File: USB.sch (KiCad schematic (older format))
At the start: 74 parts, among them J10 10103594-0001LF, Q14 BSS138LT1G, Q18 BSS138LT1G, Q24 BSS138LT1G, Q6 BSS138LT1G, U15 SN74AVC2T245RSWR, U21 M93C46-WMN6TP, U22 TLV62565DBVT, U23 FT4232H-56Q, U24 SN74AVC2T245RSWR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

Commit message: fixed bugs
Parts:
- D13: symbol AMC_FMC_Carrier-PcbDoc-rescue:PRTR5V0U2X-Diodes-AMC_FMC_Carrier-PcbDoc-rescue-AMC_FMC_Carrier-PcbDoc-rescue -> AMC_FMC_Carrier-PcbDoc-rescue:PRTR5V0U2X-Diodes-AMC_FMC_Carrier-PcbDoc-rescue-AMC_FMC_Carrier-PcbDoc-rescue-AMC_FMC_Car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
- J10: symbol AMC_FMC_Carrier-PcbDoc-rescue:HIROSE_ZX62RD-AB-5P8-Miscellaneous-AMC_FMC_Carrier-PcbDoc-rescue-AMC_FMC_Carrier-PcbDoc-rescue-AMC_FMC_Carrier-PcbDoc-rescue -> AMC_FMC_Carrier-PcbDoc-rescue:HIROSE_ZX62RD-AB-5P8-Miscellaneous-AMC_FMC_Carrier-PcbDoc-rescue-AMC_FMC_Carrier-PcbDoc-rescue-AMC_FMC_Carrier-PcbDoc-rescue-AMC_FMC_Carrier-PcbDoc-rescue
- U21: symbol AMC_FMC_Carrier-PcbDoc-rescue:M93C46-WMN6TP-Logic-AMC_FMC_Carrier-PcbDoc-rescue-AMC_FMC_Carrier-PcbDoc-rescue -> AMC_FMC_Carrier-PcbDoc-rescue:M93C46-WMN6TP-Logic-AMC_FMC_Carrier-PcbDoc-rescue-AMC_FMC_Carrier-PcbDoc-rescue-AMC_FMC_C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

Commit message: Automated edit to move cache / rescue symbols to actual eeschem library
Results of running dissect_lib3.py, not posted here
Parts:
- D13: symbol AMC_FMC_Carrier-PcbDoc-rescue:PRTR5V0U2X-Diodes-AMC_FMC_Carrier-PcbDoc-rescue-AMC_FMC_Carrier-PcbDoc-rescue-AMC_FMC_Car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 -> marble_misc:PRTR5V0U2X-Diodes
- J10: symbol AMC_FMC_Carrier-PcbDoc-rescue:HIROSE_ZX62RD-AB-5P8-Miscellaneous-AMC_FMC_Carrier-PcbDoc-rescue-AMC_FMC_Carrier-PcbDoc-r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 -> marble_misc:HIROSE_ZX62RD-AB-5P8-Miscellaneous
- U21: symbol AMC_FMC_Carrier-PcbDoc-rescue:M93C46-WMN6TP-Logic-AMC_FMC_Carrier-PcbDoc-rescue-AMC_FMC_Carrier-PcbDoc-rescue-AMC_FMC_C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 -> marble_misc:M93C46-WMN6TP-Logic
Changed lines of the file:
@@
 $EndDescr
 $Comp
-L AMC_FMC_Carrier-PcbDoc-rescue:HIROSE_ZX62RD-AB-5P8-Miscellaneous-AMC_FMC_Carrier-PcbDoc-rescue-AMC_FMC_Carrier-PcbDoc-rescue-AMC_FMC_Carrier-PcbDoc-rescue-AMC_FMC_Carrier-PcbDoc-rescue J10
+L marble_misc:HIROSE_ZX62RD-AB-5P8-Miscellaneous J10
 U 1 1 5BEB92E1
 P 1700 3500
@@
 $EndComp
 $Comp
-L AMC_FMC_Carrier-PcbDoc-rescue:+1V8_USB-powerMG-AMC_FMC_Carrier-PcbDoc-rescue-AMC_FMC_Carrier-PcbDoc-rescue-AMC_FMC_Carrier-PcbDoc-rescue-AMC_FMC_Carrier-PcbDoc-rescue #PWR0296
+L marble_misc:+1V8_USB #PWR0296
 U 1 1 5BEBDA76
 P 5900 3250
@@
 	7250 9150 7200 9150
 $Comp
-L power2:+3.3P #PWR0321
+L power:+3.3P #PWR0321
 U 1 1 5C2AA1F5
 P 5650 8850
@@
 	4050 7150 4350 7150
 $Comp
-L AMC_FMC_Carrier-PcbDoc-rescue:PRTR5V0U2X-Diodes-AMC_FMC_Carrier-PcbDoc-rescue-AMC_FMC_Carrier-PcbDoc-rescue-AMC_FMC_Carrier-PcbDoc-rescue D13
+L marble_misc:PRTR5V0U2X-Diodes D13
 U 1 1 5E04F663
 P 2400 5400
@@
 Connection ~ 4350 4700
 $Comp
-L AMC_FMC_Carrier-PcbDoc-rescue:M93C46-WMN6TP-Logic-AMC_FMC_Carrier-PcbDoc-rescue-AMC_FMC_Carrier-PcbDoc-rescue-AMC_FMC_Carrier-PcbDoc-rescue U21
+L marble_misc:M93C46-WMN6TP-Logic U21
 U 1 1 5C74B2C9
 P 3250 6850
@@
 	10000 8950 10050 8950
 $Comp
-L power2:+3.3P #PWR0153
+L power:+3.3P #PWR0153
 U 1 1 5D36D9A1
 P 10800 1400
@@
 $EndComp
 $Comp
-L power2:+3.3P #PWR0226
+L power:+3.3P #PWR0226
 U 1 1 5D38A959
 P 6550 10100
@@
 $EndComp
 $Comp
-L power2:+3.3P #PWR0230
+L power:+3.3P #PWR0230
 U 1 1 5D3A7995
 P 10700 9300
@@
 $EndComp
 $Comp
-L power2:+3.3P #PWR0310
+L power:+3.3P #PWR0310
 U 1 1 5D3C48CF
 P 7250 9750
@@
 $EndComp
 $Comp
-L power2:+3.3P #PWR0313
+L power:+3.3P #PWR0313
 U 1 1 5D41BA91
 P 10000 8950
@@
 $EndComp
 $Comp
-L AMC_FMC_Carrier-PcbDoc-rescue:+3V3_USB-AMC_FMC_Carrier-PcbDoc-rescue-AMC_FMC_Carrier-PcbDoc-rescue-AMC_FMC_Carrier-PcbDoc-rescue-AMC_FMC_Carrier-PcbDoc-rescue #PWR0275
+L marble_misc:+3V3_USB #PWR0275
 U 1 1 5E0639EB
 P 5900 1850
@@
 $EndComp
 $Comp
-L AMC_FMC_Carrier-PcbDoc-rescue:+3V3_USB-AMC_FMC_Carrier-PcbDoc-rescue-AMC_FMC_Carrier-PcbDoc-rescue-AMC_FMC_Carrier-PcbDoc-rescue-AMC_FMC_Carrier-PcbDoc-rescue #PWR0277
+L marble_misc:+3V3_USB #PWR0277
 U 1 1 5E0910B1
 P 6350 3300
@@
 $EndComp
 $Comp
-L AMC_FMC_Carrier-PcbDoc-rescue:+3V3_USB-AMC_FMC_Carrier-PcbDoc-rescue-AMC_FMC_Carrier-PcbDoc-rescue-AMC_FMC_Carrier-PcbDoc-rescue-AMC_FMC_Carrier-PcbDoc-rescue #PWR0279
+L marble_misc:+3V3_USB #PWR0279
 U 1 1 5E0AE015
 P 8300 2950
@@
 $EndComp
 $Comp
-L AMC_FMC_Carrier-PcbDoc-rescue:+3V3_USB-AMC_FMC_Carrier-PcbDoc-rescue-AMC_FMC_Carrier-PcbDoc-rescue-AMC_FMC_Carrier-PcbDoc-rescue-AMC_FMC_Carrier-PcbDoc-rescue #PWR0281
+L marble_misc:+3V3_USB #PWR0281
 U 1 1 5E0CAFF4
 P 11300 1500
@@
 $EndComp
 $Comp
-L AMC_FMC_Carrier-PcbDoc-rescue:+3V3_USB-AMC_FMC_Carrier-PcbDoc-rescue-AMC_FMC_Carrier-PcbDoc-rescue-AMC_FMC_Carrier-PcbDoc-rescue-AMC_FMC_Carrier-PcbDoc-rescue #PWR0282
+L marble_misc:+3V3_USB #PWR0282
 U 1 1 5E0E7F6F
 P 11550 2700
@@
 $EndComp
 $Comp
-L AMC_FMC_Carrier-PcbDoc-rescue:+3V3_USB-AMC_FMC_Carrier-PcbDoc-rescue-AMC_FMC_Carrier-PcbDoc-rescue-AMC_FMC_Carrier-PcbDoc-rescue-AMC_FMC_Carrier-PcbDoc-rescue #PWR0284
+L marble_misc:+3V3_USB #PWR0284
 U 1 1 5E1142BD
 P 11300 3450
@@
 $EndComp
 $Comp
-L AMC_FMC_Carrier-PcbDoc-rescue:+3V3_USB-AMC_FMC_Carrier-PcbDoc-rescue-AMC_FMC_Carrier-PcbDoc-rescue-AMC_FMC_Carrier-PcbDoc-rescue-AMC_FMC_Carrier-PcbDoc-rescue #PWR0285
+L marble_misc:+3V3_USB #PWR0285
 U 1 1 5E131666
 P 11300 2250
@@
 $EndComp
 $Comp
-L AMC_FMC_Carrier-PcbDoc-rescue:+3V3_USB-AMC_FMC_Carrier-PcbDoc-rescue-AMC_FMC_Carrier-PcbDoc-rescue-AMC_FMC_Carrier-PcbDoc-rescue-AMC_FMC_Carrier-PcbDoc-rescue #PWR0294
+L marble_misc:+3V3_USB #PWR0294
 U 1 1 5E14E7E2
 P 11300 4200
@@
 $EndComp
 $Comp
-L AMC_FMC_Carrier-PcbDoc-rescue:+3V3_USB-AMC_FMC_Carrier-PcbDoc-rescue-AMC_FMC_Carrier-PcbDoc-rescue-AMC_FMC_Carrier-PcbDoc-rescue-AMC_FMC_Carrier-PcbDoc-rescue #PWR0304
+L marble_misc:+3V3_USB #PWR0304
 U 1 1 5E16BA3D
 P 11550 4650
@@
 $EndComp
 $Comp
-L AMC_FMC_Carrier-PcbDoc-rescue:+3V3_USB-AMC_FMC_Carrier-PcbDoc-rescue-AMC_FMC_Carrier-PcbDoc-rescue-AMC_FMC_Carrier-PcbDoc-rescue-AMC_FMC_Carrier-PcbDoc-rescue #PWR0306
+L marble_misc:+3V3_USB #PWR0306
 U 1 1 5E1A590C
 P 13600 7250
@@
 $EndComp
 $Comp
-L AMC_FMC_Carrier-PcbDoc-rescue:+3V3_USB-AMC_FMC_Carrier-PcbDoc-rescue-AMC_FMC_Carrier-PcbDoc-rescue-AMC_FMC_Carrier-PcbDoc-rescue-AMC_FMC_Carrier-PcbDoc-rescue #PWR0307
+L marble_misc:+3V3_USB #PWR0307
 U 1 1 5E1B4270
 P 13250 6100
@@
 $EndComp
 $Comp
-L AMC_FMC_Carrier-PcbDoc-rescue:+3V3_USB-AMC_FMC_Carrier-PcbDoc-rescue-AMC_FMC_Carrier-PcbDoc-rescue-AMC_FMC_Carrier-PcbDoc-rescue-AMC_FMC_Carrier-PcbDoc-rescue #PWR0309
+L marble_misc:+3V3_USB #PWR0309
 U 1 1 5E1C2F5B
 P 13350 6800
@@
 	13250 6100 13400 6100
 $Comp
-L AMC_FMC_Carrier-PcbDoc-rescue:+3V3_USB-AMC_FMC_Carrier-PcbDoc-rescue-AMC_FMC_Carrier-PcbDoc-rescue-AMC_FMC_Carrier-PcbDoc-rescue-AMC_FMC_Carrier-PcbDoc-rescue #PWR0311
+L marble_misc:+3V3_USB #PWR0311
 U 1 1 5E1E0E93
 P 11300 7050
@@
 $EndComp
 $Comp
-L AMC_FMC_Carrier-PcbDoc-rescue:+3V3_USB-AMC_FMC_Carrier-PcbDoc-rescue-AMC_FMC_Carrier-PcbDoc-rescue-AMC_FMC_Carrier-PcbDoc-rescue-AMC_FMC_Carrier-PcbDoc-rescue #PWR0316
+L marble_misc:+3V3_USB #PWR0316
 U 1 1 5E20CA7E
 P 11300 7650
@@
 $EndComp
 $Comp
-L AMC_FMC_Carrier-PcbDoc-rescue:+3V3_USB-AMC_FMC_Carrier-PcbDoc-rescue-AMC_FMC_Carrier-PcbDoc-rescue-AMC_FMC_Carrier-PcbDoc-rescue-AMC_FMC_Carrier-PcbDoc-rescue #PWR0319
+L marble_misc:+3V3_USB #PWR0319
 U 1 1 5E24786F
 P 10050 8150
@@
 $EndComp
 $Comp
-L AMC_FMC_Carrier-PcbDoc-rescue:+3V3_USB-AMC_FMC_Carrier-PcbDoc-rescue-AMC_FMC_Carrier-PcbDoc-rescue-AMC_FMC_Carrier-PcbDoc-rescue-AMC_FMC_Carrier-PcbDoc-rescue #PWR0325
+L marble_misc:+3V3_USB #PWR0325
 U 1 1 5E28111D
 P 10000 8850
@@
 $EndComp
 $Comp
-L AMC_FMC_Carrier-PcbDoc-rescue:+3V3_USB-AMC_FMC_Carrier-PcbDoc-rescue-AMC_FMC_Carrier-PcbDoc-rescue-AMC_FMC_Carrier-PcbDoc-rescue-AMC_FMC_Carrier-PcbDoc-rescue #PWR0327
+L marble_misc:+3V3_USB #PWR0327
 U 1 1 5E29D842
 P 7200 8950
@@
 $EndComp
 $Comp
-L AMC_FMC_Carrier-PcbDoc-rescue:+3V3_USB-AMC_FMC_Carrier-PcbDoc-rescue-AMC_FMC_Carrier-PcbDoc-rescue-AMC_FMC_Carrier-PcbDoc-rescue-AMC_FMC_Carrier-PcbDoc-rescue #PWR0328
+L marble_misc:+3V3_USB #PWR0328
 U 1 1 5E2AB899
 P 7200 9050
@@
 $EndComp
 $Comp
-L AMC_FMC_Carrier-PcbDoc-rescue:+3V3_USB-AMC_FMC_Carrier-PcbDoc-rescue-AMC_FMC_Carrier-PcbDoc-rescue-AMC_FMC_Carrier-PcbDoc-rescue-AMC_FMC_Carrier-PcbDoc-rescue #PWR0330
+L marble_misc:+3V3_USB #PWR0330
 U 1 1 5E2C78AB
 P 7250 9650
@@
 $EndComp
 $Comp
-L AMC_FMC_Carrier-PcbDoc-rescue:+3V3_USB-AMC_FMC_Carrier-PcbDoc-rescue-AMC_FMC_Carrier-PcbDoc-rescue-AMC_FMC_Carrier-PcbDoc-rescue-AMC_FMC_Carrier-PcbDoc-rescue #PWR0332
+L marble_misc:+3V3_USB #PWR0332
 U 1 1 5E2E3981
 P 11550 8100
@@
 $EndComp
 $Comp
-L AMC_FMC_Carrier-PcbDoc-rescue:+3V3_USB-AMC_FMC_Carrier-PcbDoc-rescue-AMC_FMC_Carrier-PcbDoc-rescue-AMC_FMC_Carrier-PcbDoc-rescue-AMC_FMC_Carrier-PcbDoc-rescue #PWR0335
+L marble_misc:+3V3_USB #PWR0335
 U 1 1 5E30DBBE
 P 10250 9300
@@
 $EndComp
 $Comp
-L AMC_FMC_Carrier-PcbDoc-rescue:+3V3_USB-AMC_FMC_Carrier-PcbDoc-rescue-AMC_FMC_Carrier-PcbDoc-rescue-AMC_FMC_Carrier-PcbDoc-rescue-AMC_FMC_Carrier-PcbDoc-rescue #PWR0337
+L marble_misc:+3V3_USB #PWR0337
 U 1 1 5E329CA2
 P 7000 10100
@@
 $EndComp
 $Comp
-L AMC_FMC_Carrier-PcbDoc-rescue:+3V3_USB-AMC_FMC_Carrier-PcbDoc-rescue-AMC_FMC_Carrier-PcbDoc-rescue-AMC_FMC_Carrier-PcbDoc-rescue-AMC_FMC_Carrier-PcbDoc-rescue #PWR0339
+L marble_misc:+3V3_USB #PWR0339
 U 1 1 5E345D17
 P 5200 8000
@@
 Connection ~ 5200 8000
 $Comp
-L AMC_FMC_Carrier-PcbDoc-rescue:+3V3_USB-AMC_FMC_Carrier-PcbDoc-rescue-AMC_FMC_Carrier-PcbDoc-rescue-AMC_FMC_Carrier-PcbDoc-rescue-AMC_FMC_Carrier-PcbDoc-rescue #PWR0341
+L marble_misc:+3V3_USB #PWR0341
 U 1 1 5E37DE16
 P 5200 7200
@@
 $EndComp
 $Comp
-L AMC_FMC_Carrier-PcbDoc-rescue:+3V3_USB-AMC_FMC_Carrier-PcbDoc-rescue-AMC_FMC_Carrier-PcbDoc-rescue-AMC_FMC_Carrier-PcbDoc-rescue-AMC_FMC_Carrier-PcbDoc-rescue #PWR0343
+L marble_misc:+3V3_USB #PWR0343
 U 1 1 5E399F01
 P 4900 6500
@@
 $EndComp
 $Comp
-L AMC_FMC_Carrier-PcbDoc-rescue:+3V3_USB-AMC_FMC_Carrier-PcbDoc-rescue-AMC_FMC_Carrier-PcbDoc-rescue-AMC_FMC_Carrier-PcbDoc-rescue-AMC_FMC_Carrier-PcbDoc-rescue #PWR0478
+L marble_misc:+3V3_USB #PWR0478
 U 1 1 5E3B5F64
 P 4900 5800
@@
 $EndComp
 $Comp
-L AMC_FMC_Carrier-PcbDoc-rescue:+3V3_USB-AMC_FMC_Carrier-PcbDoc-rescue-AMC_FMC_Carrier-PcbDoc-rescue-AMC_FMC_Carrier-PcbDoc-rescue-AMC_FMC_Carrier-PcbDoc-rescue #PWR0479
+L marble_misc:+3V3_USB #PWR0479
 U 1 1 5E3DFF47
 P 4050 6550
@@
 $EndComp
 $Comp
-L AMC_FMC_Carrier-PcbDoc-rescue:+3V3_USB-AMC_FMC_Carrier-PcbDoc-rescue-AMC_FMC_Carrier-PcbDoc-rescue-AMC_FMC_Carrier-PcbDoc-rescue-AMC_FMC_Carrier-PcbDoc-rescue #PWR0480
+L marble_misc:+3V3_USB #PWR0480
 U 1 1 5E3EE00F
 P 3450 6200
@@
 $EndComp
 $Comp
-L AMC_FMC_Carrier-PcbDoc-rescue:+3V3_USB-AMC_FMC_Carrier-PcbDoc-rescue-AMC_FMC_Carrier-PcbDoc-rescue-AMC_FMC_Carrier-PcbDoc-rescue-AMC_FMC_Carrier-PcbDoc-rescue #PWR0599
+L marble_misc:+3V3_USB #PWR0599
 U 1 1 5E40A0AB
 P 3650 7250
@@
 $EndComp
 $Comp
-L AMC_FMC_Carrier-PcbDoc-rescue:+3V3_USB-AMC_FMC_Carrier-PcbDoc-rescue-AMC_FMC_Carrier-PcbDoc-rescue-AMC_FMC_Carrier-PcbDoc-rescue-AMC_FMC_Carrier-PcbDoc-rescue #PWR0601
+L marble_misc:+3V3_USB #PWR0601
 U 1 1 5E4346A3
 P 8000 8800
@@
 	5650 9200 5650 9350
 $Comp
-L power2:+3.3P #PWR0647
+L power:+3.3P #PWR0647
 U 1 1 5CDA74D2
 P 6000 8850
@@
 Connection ~ 6000 9450
 $Comp
-L AMC_FMC_Carrier-PcbDoc-rescue:+3V3_USB-AMC_FMC_Carrier-PcbDoc-rescue-AMC_FMC_Carrier-PcbDoc-rescue-AMC_FMC_Carrier-PcbDoc-rescue-AMC_FMC_Carrier-PcbDoc-rescue #PWR0643
+L marble_misc:+3V3_USB #PWR0643
 U 1 1 5CE79DFD
 P 5150 9500
@@
 Connection ~ 5150 10550
 $Comp
-L AMC_FMC_Carrier-PcbDoc-rescue:+3V3_USB-AMC_FMC_Carrier-PcbDoc-rescue-AMC_FMC_Carrier-PcbDoc-rescue-AMC_FMC_Carrier-PcbDoc-rescue-AMC_FMC_Carrier-PcbDoc-rescue #PWR0645
+L marble_misc:+3V3_USB #PWR0645
 U 1 1 5D07178D
 P 5700 10550

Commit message: 16 warnings, 16 errors
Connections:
- no-connect marks 25 -> 27
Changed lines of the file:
@@
 Wire Wire Line
 	8650 4500 8650 9200
+NoConn ~ 8000 6300
+NoConn ~ 8000 6500
 $EndSCHEMATC

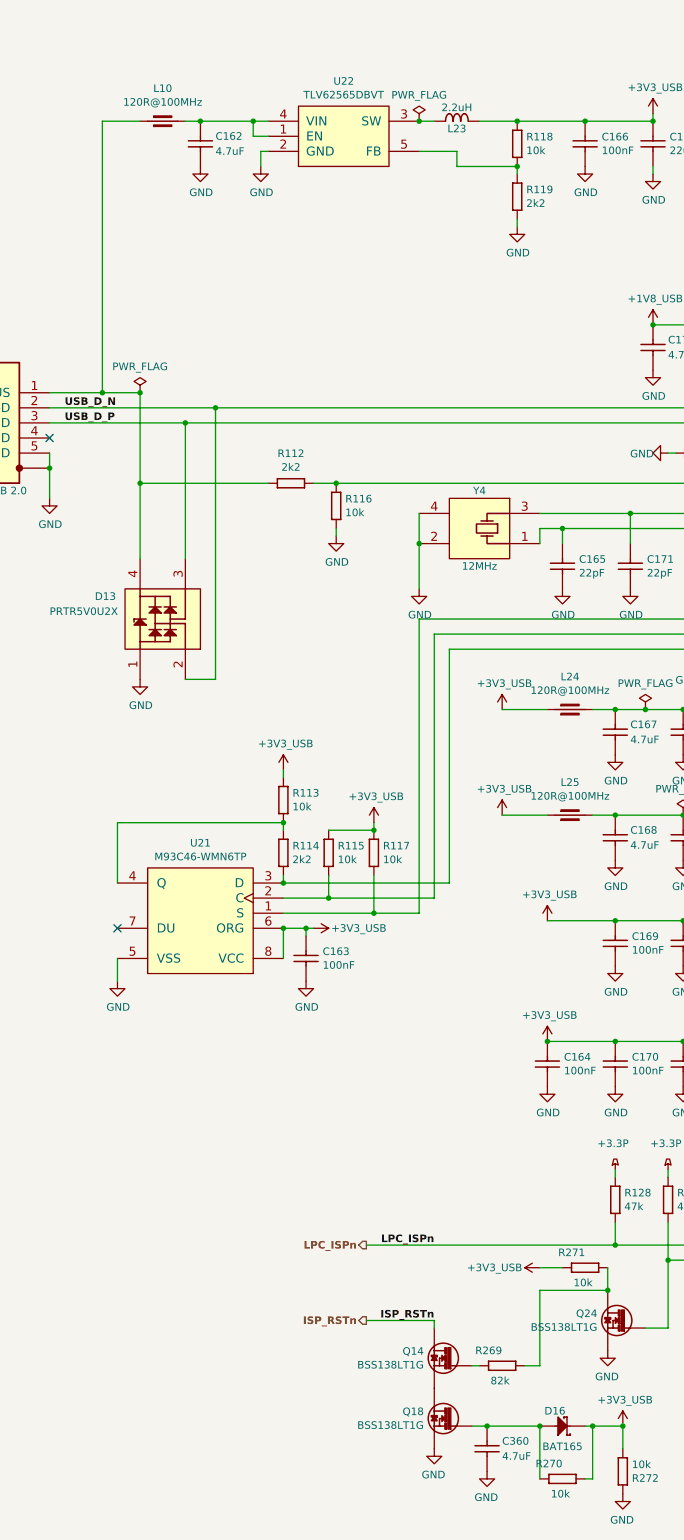
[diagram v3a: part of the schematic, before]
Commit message: shave ERC report down to 5 issues
  * mostly by adding power inputs / outputs to the symbols (many
    power pins were set to bidirectional, which causes issues)
  * remove some stray power symbols which were not connected to
    anything
  * FMC connector: change all VCC and GND pins to Power input type
    (there's a lot of them!!)
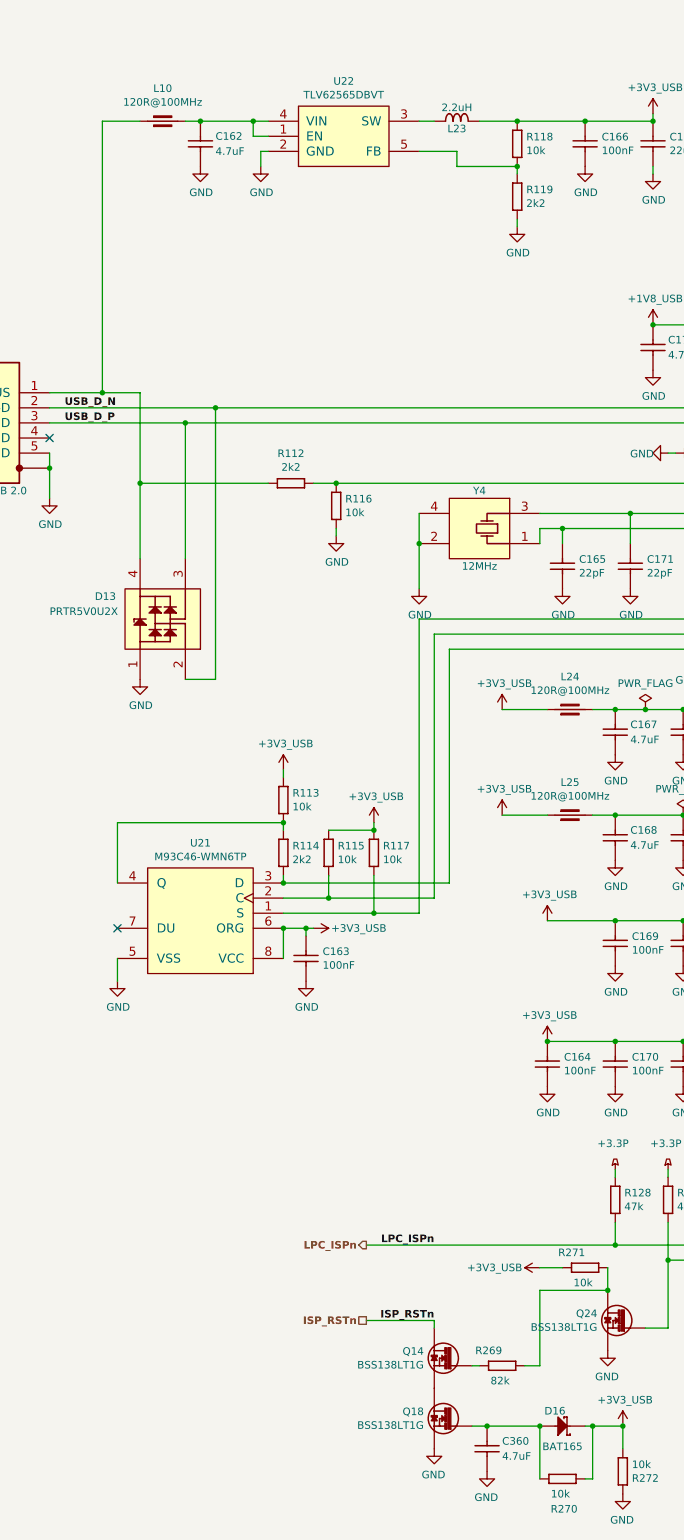
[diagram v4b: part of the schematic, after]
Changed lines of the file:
@@
 Wire Wire Line
 	2350 7450 2350 7600
-Text HLabel 4000 9850 0    50   Output ~ 10
+Text HLabel 4000 9850 0    50   UnSpc ~ 10
 ISP_RSTn
 Text HLabel 4000 9350 0    50   Output ~ 10
@@
 AR Path="/5CA40231/5CFD7948" Ref="R?"  Part="1"
 AR Path="/5C16C03C/5CFD7948" Ref="R270"  Part="1"
-F 0 "R270" H 5600 10800 50  0000 L CNN
+F 0 "R270" H 5500 11100 50  0000 L CNN
 F 1 "R0402_10K_1%_0.0625W_100PPM" H 5450 10690 60  0001 L CNN
 F 2 "RESC1005X40N" H 5450 9880 60  0001 L CNN
@@
 $EndComp
 Connection ~ 10050 8850
-$Comp
-L power:PWR_FLAG #FLG?
-U 1 1 5D3ED707
-P 2500 3700
-AR Path="/5BABAC65/5D3ED707" Ref="#FLG?"  Part="1"
-AR Path="/5C16C03C/5D3ED707" Ref="#FLG0126"  Part="1"
-F 0 "#FLG0126" H 2500 3775 50  0001 C CNN
-F 1 "PWR_FLAG" H 2500 3873 50  0000 C CNN
-F 2 "" H 2500 3700 50  0001 C CNN
-F 3 "~" H 2500 3700 50  0001 C CNN
-	1    2500 3700
-	1    0    0    -1
-$EndComp
-Connection ~ 2500 3700
-$Comp
-L power:PWR_FLAG #FLG?
-U 1 1 5D3FE99C
-P 4350 1900
-AR Path="/5BABAC65/5D3FE99C" Ref="#FLG?"  Part="1"
-AR Path="/5C16C03C/5D3FE99C" Ref="#FLG0127"  Part="1"
-F 0 "#FLG0127" H 4350 1975 50  0001 C CNN
-F 1 "PWR_FLAG" H 4350 2073 50  0000 C CNN
-F 2 "" H 4350 1900 50  0001 C CNN
-F 3 "~" H 4350 1900 50  0001 C CNN
-	1    4350 1900
-	1    0    0    -1
-$EndComp
-Connection ~ 4350 1900
 Wire Wire Line
 	5900 2200 5900 2250
